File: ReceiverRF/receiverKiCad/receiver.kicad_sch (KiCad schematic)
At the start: 23 parts, among them J2 Conn_01x05_Socket, U1 STM32F103RET6, Y1 YG8M000000S418

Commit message: changement cristal
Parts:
- Y1: value YG8M000000S418 -> CTX853CT-ND; Digikey 3372-YG8M000000S418TR-ND -> CTX853CT-ND
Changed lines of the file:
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@@
 			)
 		)
-		(property "Value" "YG8M000000S418"
+		(property "Value" "CTX853CT-ND"
 			(at 238.76 118.11 0)
 			(effects
@@
 			)
 		)
-		(property "Datasheet" "https://www.digikey.ca/en/products/detail/nextgen-components/YG8M000000S416/17289334"
+		(property "Datasheet" "https://www.digikey.ca/en/products/detail/cts-frequency-controls/406C35D08M00000/2292774"
 			(at 238.76 125.73 0)
 			(effects
@@
 			)
 		)
-		(property "Description" "YG8M000000S416"
+		(property "Description" "406C35D08M00000"
 			(at 238.76 125.73 0)
 			(effects
@@
 			)
 		)
-		(property "Digikey" "  3372-YG8M000000S418TR-ND"
+		(property "Digikey" "CTX853CT-ND"
 			(at 238.76 125.73 0)
 			(effects

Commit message: changement vers footprint 1206
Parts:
- CSTL_C1, CSTL_C2, STM_C1, STM_C3, STM_C4, STM_C5, S_C10, S_C2, S_C7: footprint Capacitor_SMD:C_0402_1005Metric -> Capacitor_SMD:C_1206_3216Metric
- I2C_R1, I2C_R2, STM_R2, STM_R3, S_R1, S_R4: footprint Resistor_SMD:R_0402_1005Metric -> Resistor_SMD:R_1206_3216Metric
- STM_C8, STM_C9: footprint Capacitor_SMD:C_0603_1608Metric -> Capacitor_SMD:C_1206_3216Metric
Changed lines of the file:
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@@
 			)
 		)
-		(property "Footprint" "Resistor_SMD:R_0402_1005Metric"
+		(property "Footprint" "Resistor_SMD:R_1206_3216Metric"
 			(at 240.03 93.218 90)
 			(effects
@@
 			)
 		)
-		(property "Footprint" "Capacitor_SMD:C_0402_1005Metric"
+		(property "Footprint" "Capacitor_SMD:C_1206_3216Metric"
 			(at 248.6152 138.43 0)
 			(effects
@@
 			)
 		)
-		(property "Footprint" "Resistor_SMD:R_0402_1005Metric"
+		(property "Footprint" "Resistor_SMD:R_1206_3216Metric"
 			(at 107.95 56.388 90)
 			(effects
@@
 			)
 		)
-		(property "Footprint" "Resistor_SMD:R_0402_1005Metric"
+		(property "Footprint" "Resistor_SMD:R_1206_3216Metric"
 			(at 230.632 59.69 90)
 			(effects
@@
 			)
 		)
-		(property "Footprint" "Capacitor_SMD:C_0402_1005Metric"
+		(property "Footprint" "Capacitor_SMD:C_1206_3216Metric"
 			(at 97.4852 44.45 0)
 			(effects
@@
 			)
 		)
-		(property "Footprint" "Capacitor_SMD:C_0402_1005Metric"
+		(property "Footprint" "Capacitor_SMD:C_1206_3216Metric"
 			(at 107.6452 44.45 0)
 			(effects
@@
 			)
 		)
-		(property "Footprint" "Resistor_SMD:R_0402_1005Metric"
+		(property "Footprint" "Resistor_SMD:R_1206_3216Metric"
 			(at 244.602 99.06 90)
 			(effects
@@
 			)
 		)
-		(property "Footprint" "Capacitor_SMD:C_0402_1005Metric"
+		(property "Footprint" "Capacitor_SMD:C_1206_3216Metric"
 			(at 232.1052 138.43 0)
 			(effects
@@
 			)
 		)
-		(property "Footprint" "Capacitor_SMD:C_0603_1608Metric"
+		(property "Footprint" "Capacitor_SMD:C_1206_3216Metric"
 			(at 197.8152 44.45 0)
 			(effects
@@
 			)
 		)
-		(property "Footprint" "Capacitor_SMD:C_0603_1608Metric"
+		(property "Footprint" "Capacitor_SMD:C_1206_3216Metric"
 			(at 177.4952 44.45 0)
 			(effects
@@
 			)
 		)
-		(property "Footprint" "Capacitor_SMD:C_0402_1005Metric"
+		(property "Footprint" "Capacitor_SMD:C_1206_3216Metric"
 			(at 117.8052 44.45 0)
 			(effects
@@
 			)
 		)
-		(property "Footprint" "Resistor_SMD:R_0402_1005Metric"
+		(property "Footprint" "Resistor_SMD:R_1206_3216Metric"
 			(at 254 127.508 90)
 			(effects
@@
 			)
 		)
-		(property "Footprint" "Capacitor_SMD:C_0402_1005Metric"
+		(property "Footprint" "Capacitor_SMD:C_1206_3216Metric"
 			(at 168.6052 44.45 0)
 			(effects
@@
 			)
 		)
-		(property "Footprint" "Capacitor_SMD:C_0402_1005Metric"
+		(property "Footprint" "Capacitor_SMD:C_1206_3216Metric"
 			(at 116.5352 62.23 0)
 			(effects
@@
 			)
 		)
-		(property "Footprint" "Capacitor_SMD:C_0402_1005Metric"
+		(property "Footprint" "Capacitor_SMD:C_1206_3216Metric"
 			(at 87.3252 44.45 0)
 			(effects
@@
 			)
 		)
-		(property "Footprint" "Capacitor_SMD:C_0402_1005Metric"
+		(property "Footprint" "Capacitor_SMD:C_1206_3216Metric"
 			(at 127.9652 44.45 0)
 			(effects
@@
 			)
 		)
-		(property "Footprint" "Resistor_SMD:R_0402_1005Metric"
+		(property "Footprint" "Resistor_SMD:R_1206_3216Metric"
 			(at 240.792 59.69 90)
 			(effects

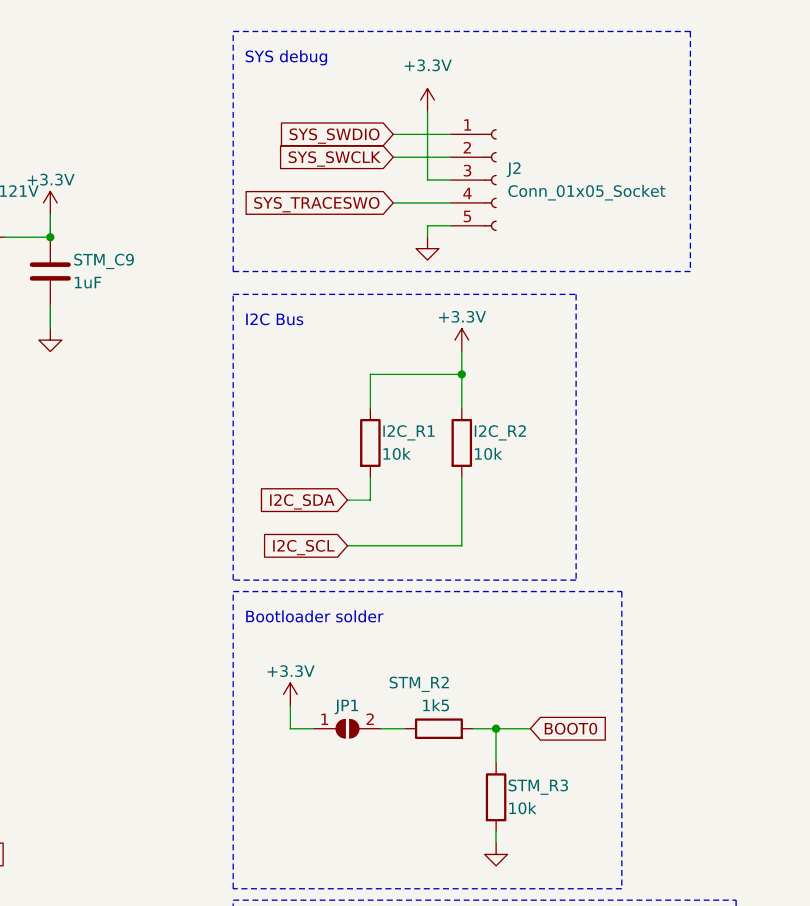
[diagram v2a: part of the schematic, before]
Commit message: changement BOM et choix nouvelles pièces 1206
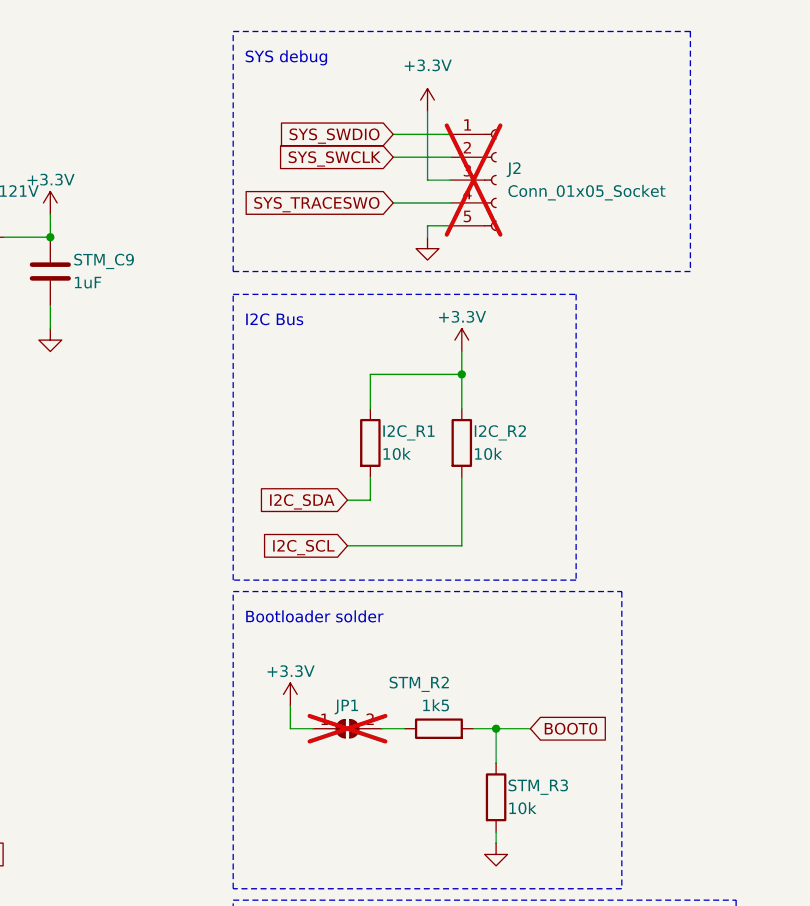
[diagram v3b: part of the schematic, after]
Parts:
- CSTL_C1, CSTL_C2: footprint Capacitor_SMD:C_1206_3216Metric -> Capacitor_SMD:C_0603_1608Metric_Pad1.08x0.95mm_HandSolder; Digikey 478-11769-1-ND -> 399-CBR06C160F5GACCT-ND
- I2C_R1, I2C_R2, STM_R3, S_R1: Digikey 311-10KJRCT-ND -> 311-10.0KFRCT-ND
- J2, JP1: now not fitted
- STM_C1, STM_C3, STM_C4, STM_C5, S_C10, S_C2: Digikey 2679-AGC0402X7R500-104KNPTR-ND -> 399-C1206C104K5RACTUCT-ND
- STM_C8, STM_C9: Digikey 2679-AGC0603X7R250-105KXPTR-ND -> 1276-1068-1-ND
- STM_R2: Digikey P1.5KDCCT-ND -> 541-4184-1-ND
- S_C7: Digikey 2679-AGC0402X7R500-103KNPTR-ND -> 311-1174-1-ND
- S_R4: Digikey P10.0LCT-ND -> RMCF1206FT10R0CT-ND
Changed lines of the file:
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@@
 			)
 		)
-		(property "Digikey" "P1.5KDCCT-ND"
+		(property "Digikey" "541-4184-1-ND"
 			(at 240.03 91.44 0)
 			(effects
@@
 			)
 		)
-		(property "Footprint" "Capacitor_SMD:C_1206_3216Metric"
+		(property "Footprint" "Capacitor_SMD:C_0603_1608Metric_Pad1.08x0.95mm_HandSolder"
 			(at 248.6152 138.43 0)
 			(effects
@@
 			)
 		)
-		(property "Digikey" "478-11769-1-ND"
+		(property "Digikey" "399-CBR06C160F5GACCT-ND"
 			(at 247.65 134.62 0)
 			(effects
@@
 			)
 		)
-		(property "Digikey" "311-10KJRCT-ND"
+		(property "Digikey" "311-10.0KFRCT-ND"
 			(at 107.95 54.61 0)
 			(effects
@@
 		(in_bom yes)
 		(on_board yes)
-		(dnp no)
+		(dnp yes)
 		(property "Reference" "JP1"
 			(at 229.87 88.9 0)
@@
 			)
 		)
-		(property "Digikey" "311-10KJRCT-ND"
+		(property "Digikey" "311-10.0KFRCT-ND"
 			(at 232.41 59.69 0)
 			(effects
@@
 			)
 		)
-		(property "Digikey" "2679-AGC0402X7R500-104KNPTR-ND"
+		(property "Digikey" "399-C1206C104K5RACTUCT-ND"
 			(at 96.52 40.64 0)
 			(effects
@@
 			)
 		)
-		(property "Digikey" "2679-AGC0402X7R500-104KNPTR-ND"
+		(property "Digikey" "399-C1206C104K5RACTUCT-ND"
 			(at 106.68 40.64 0)
 			(effects
@@
 			)
 		)
-		(property "Digikey" "311-10KJRCT-ND"
+		(property "Digikey" "311-10.0KFRCT-ND"
 			(at 246.38 99.06 0)
 			(effects
@@
 			)
 		)
-		(property "Footprint" "Capacitor_SMD:C_1206_3216Metric"
+		(property "Footprint" "Capacitor_SMD:C_0603_1608Metric_Pad1.08x0.95mm_HandSolder"
 			(at 232.1052 138.43 0)
 			(effects
@@
 			)
 		)
-		(property "Digikey" "478-11769-1-ND"
+		(property "Digikey" "399-CBR06C160F5GACCT-ND"
 			(at 231.14 134.62 0)
 			(effects
@@
 			)
 		)
-		(property "Digikey" "  2679-AGC0603X7R250-105KXPTR-ND"
+		(property "Digikey" "1276-1068-1-ND"
 			(at 196.85 40.64 0)
 			(effects
@@
 			)
 		)
-		(property "Digikey" "  2679-AGC0603X7R250-105KXPTR-ND"
+		(property "Digikey" "1276-1068-1-ND"
 			(at 176.53 40.64 0)
 			(effects
@@
 			)
 		)
-		(property "Digikey" "2679-AGC0402X7R500-104KNPTR-ND"
+		(property "Digikey" "399-C1206C104K5RACTUCT-ND"
 			(at 116.84 40.64 0)
 			(effects
@@
 			)
 		)
-		(property "Digikey" "P10.0LCT-ND"
+		(property "Digikey" "RMCF1206FT10R0CT-ND"
 			(at 254 125.73 0)
 			(effects
@@
 			)
 		)
-		(property "Digikey" "  2679-AGC0402X7R500-103KNPTR-ND"
+		(property "Digikey" "311-1174-1-ND"
 			(at 167.64 40.64 0)
 			(effects
@@
 		(in_bom yes)
 		(on_board yes)
-		(dnp no)
+		(dnp yes)
 		(fields_autoplaced yes)
 		(property "Reference" "J2"
@@
 			)
 		)
-		(property "Digikey" "2679-AGC0402X7R500-104KNPTR-ND"
+		(property "Digikey" "399-C1206C104K5RACTUCT-ND"
 			(at 115.57 58.42 0)
 			(effects
@@
 			)
 		)
-		(property "Digikey" "2679-AGC0402X7R500-104KNPTR-ND"
+		(property "Digikey" "399-C1206C104K5RACTUCT-ND"
 			(at 86.36 40.64 0)
 			(effects
@@
 			)
 		)
-		(property "Digikey" "2679-AGC0402X7R500-104KNPTR-ND"
+		(property "Digikey" "399-C1206C104K5RACTUCT-ND"
 			(at 127 40.64 0)
 			(effects
@@
 			)
 		)
-		(property "Digikey" "311-10KJRCT-ND"
+		(property "Digikey" "311-10.0KFRCT-ND"
 			(at 242.57 59.69 0)
 			(effects

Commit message: ideFIX v2 fix schematic, layout
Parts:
- added J3: Conn_01x02_Socket, Connector_PinHeader_2.54mm:PinHeader_1x02_P2.54mm_Vertical, symbol Connector:Conn_01x02_Socket
- J2: footprint Connector_PinHeader_2.00mm:PinHeader_1x05_P2.00mm_Vertical -> Connector_PinHeader_2.54mm:PinHeader_1x05_P2.54mm_Vertical; now fitted
- JP1: now fitted
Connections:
- net BUZZER: now also U1.43 (PA10); no longer U1.41 (PA8)
- net LED1: now also U1.14 (PA0); no longer U1.43 (PA10)
- net LED2: now also U1.15 (PA1); no longer U1.44 (PA11)
- net LED3: now also U1.16 (PA2); no longer U1.45 (PA12)
- net MLX_INT: now also U1.44 (PA11); no longer U1.50 (PA15)
- net MLX_INT/TRIG: now also U1.45 (PA12); no longer U1.52 (PC11)
- net PUSH_1: now also U1.37 (PC6); no longer U1.33 (PB12)
- net PUSH_2: now also U1.38 (PC7); no longer U1.34 (PB13)
- net PUSH_3: now also U1.39 (PC8); no longer U1.35 (PB14)
- net PUSH_4: now also U1.40 (PC9); no longer U1.36 (PB15)
- net RFM_GPIO1: now also U1.27 (PB1); no longer U1.26 (PB0)
- net RFM_GPIO2: now also U1.26 (PB0); no longer U1.27 (PB1)
- net RFM_GPIO3: now also U1.25 (PC5); no longer U1.28 (PB2)
- net RFM_NIRQ: now also U1.20 (PA4); no longer U1.29 (PB10)
- net RFM_SDN: now also U1.17 (PA3); no longer U1.25 (PC5)
- net SPI_RFM_CS: now also U1.24 (PC4); no longer U1.20 (PA4)
- net UART4_TX: now reaches U1.51 (PC10)
- net UART4_TX: now also J3.1 (Pin_1)
- new net RFM_GPIO4: U1.29 (PB10)
- new net RFM_GPIO5: U1.28 (PB2)
- new net UART4_RX: J3.2 (Pin_2), U1.52 (PC11)
- no-connect marks 25 -> 12
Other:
- sheet IOinterface renamed InterfaceBoard
- sheet regulateurs renamed Power
- note added: "UART out"

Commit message: revision schematic before tracing
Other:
- company: (none) -> GAUL
- title: (none) -> IdeFIX
- moved on the sheet: CSTL_C1, CSTL_C2, I2C_R1, I2C_R2, J2, J3, JP1, STM_R2, STM_R3, S_R4, Y1

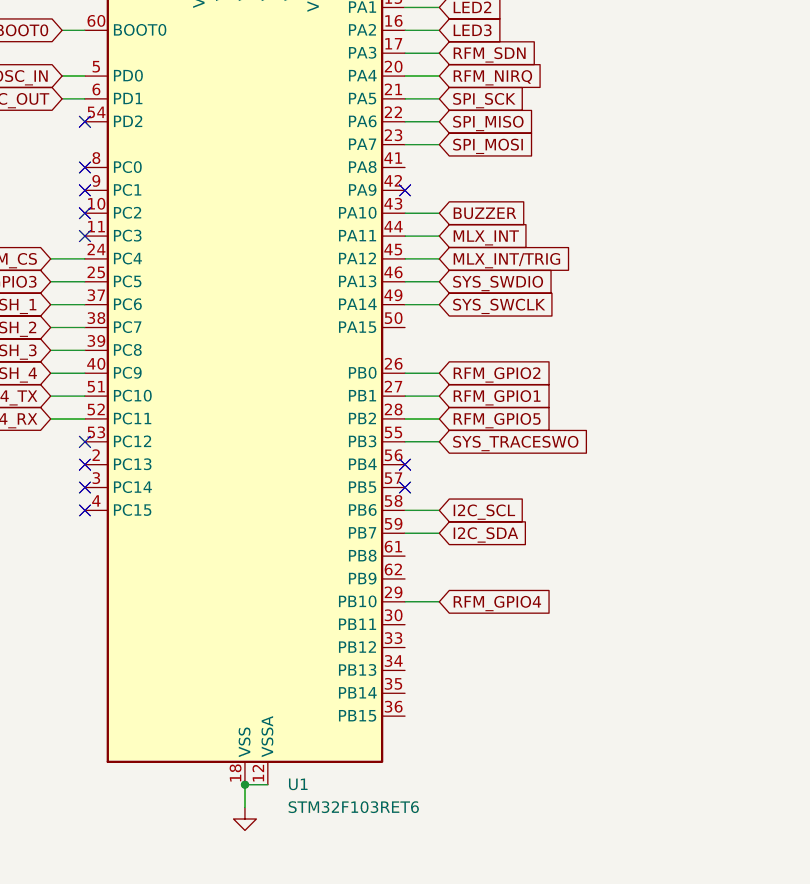
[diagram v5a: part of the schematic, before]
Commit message: fix zener diode footprint, thermal relief on SMA conn, more work on silkscreen
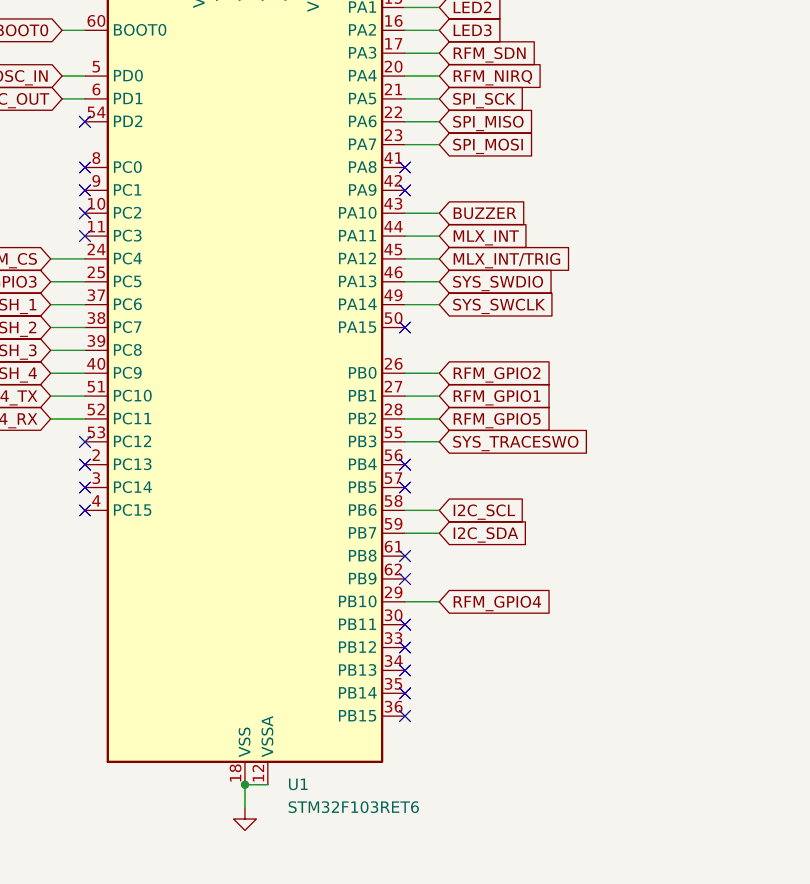
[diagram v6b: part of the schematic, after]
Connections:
- no-connect marks 12 -> 21
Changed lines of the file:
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@@
+	)
+	(no_connect
+		(at 171.45 135.89)
 	)
 	(no_connect
@@
 	)
 	(no_connect
+		(at 171.45 133.35)
+	)
+	(no_connect
+		(at 171.45 120.65)
+	)
+	(no_connect
 		(at 171.45 77.47)
+	)
+	(no_connect
+		(at 171.45 92.71)
 	)
 	(no_connect
@@
 	)
 	(no_connect
+		(at 171.45 130.81)
+	)
+	(no_connect
 		(at 171.45 110.49)
+	)
+	(no_connect
+		(at 171.45 74.93)
 	)
 	(no_connect
@@
 	)
 	(no_connect
+		(at 171.45 125.73)
+	)
+	(no_connect
 		(at 135.89 107.95)
+	)
+	(no_connect
+		(at 171.45 118.11)
 	)
 	(no_connect
@@
 	)
 	(no_connect
+		(at 171.45 128.27)
+	)
+	(no_connect

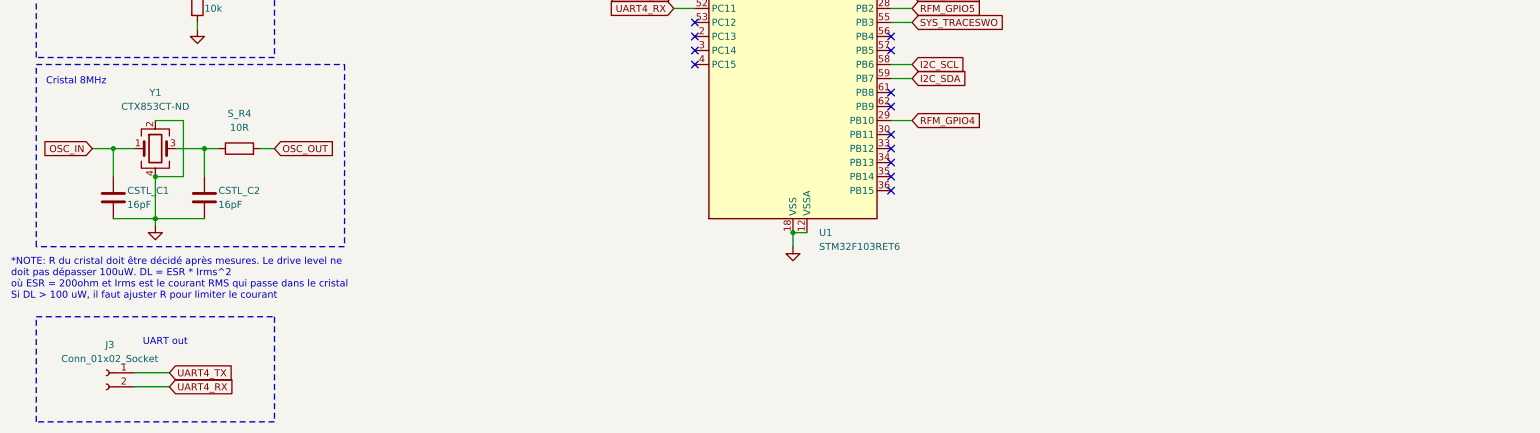
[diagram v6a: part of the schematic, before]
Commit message: 3.2mm holes, XT30 connector, add polyfuse, minor fixes
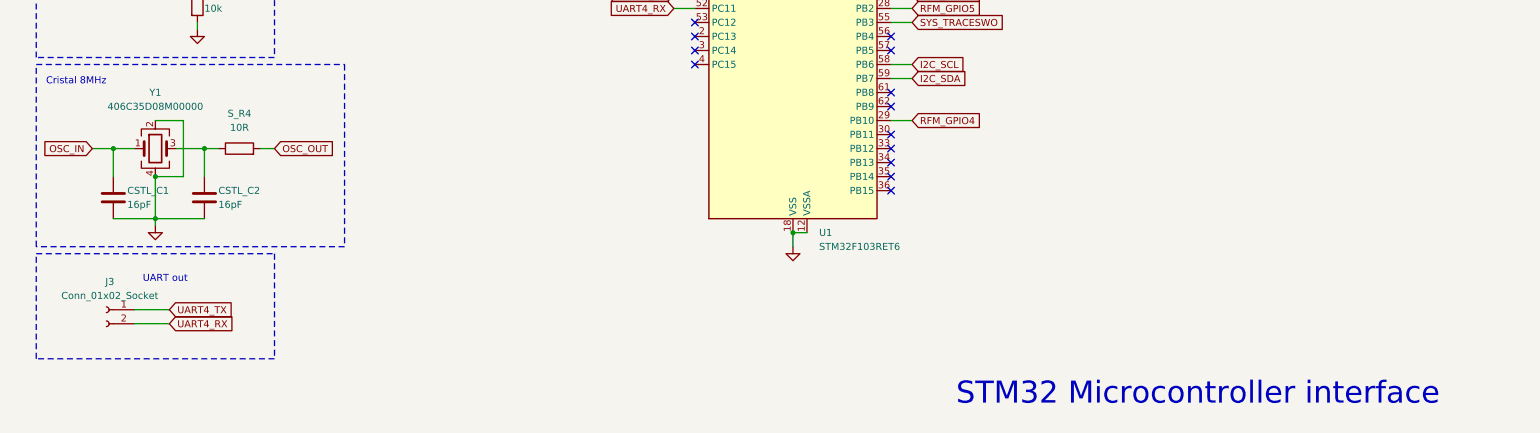
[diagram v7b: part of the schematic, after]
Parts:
- Y1: value CTX853CT-ND -> 406C35D08M00000
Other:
- note added: "STM32 Microcontroller interface"
- note removed: "*NOTE: R du cristal doit être décidé après mesures. Le drive level ne doit pas dépasser 100uW. DL = ESR * Irms^2 où ESR = 200ohm et Irms est le courant RMS qui passe dans le cristal Si DL > 100 uW, il faut ajuster R pour limiter le courant"
- moved on the sheet: J3
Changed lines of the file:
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@@
 	(wire
 		(pts
-			(xy 34.29 168.91) (xy 40.64 168.91)
+			(xy 34.29 157.48) (xy 40.64 157.48)
 		)
 		(stroke
@@
 	(wire
 		(pts
-			(xy 34.29 171.45) (xy 40.64 171.45)
+			(xy 34.29 160.02) (xy 40.64 160.02)
 		)
 		(stroke
@@
 	)
 	(rectangle
-		(start 16.51 158.75)
-		(end 59.69 177.8)
+		(start 16.51 147.32)
+		(end 59.69 166.37)
 		(stroke
 			(width 0)
@@
 		)
 	)
+	(text "STM32 Microcontroller interface"
+		(exclude_from_sim no)
+		(at 227.076 172.72 0)
+		(effects
+			(font
+				(size 4 4)
+			)
+		)
+	)
 	(text "Cristal 8MHz"
 		(exclude_from_sim no)
@@
 		)
 	)
-	(text "*NOTE: R du cristal doit être décidé après mesures. Le drive level ne\ndoit pas dépasser 100uW. DL = ESR * Irms^2\noù ESR = 200ohm et Irms est le courant RMS qui passe dans le cristal\nSi DL > 100 uW, il faut ajuster R pour limiter le courant"
-		(exclude_from_sim no)
-		(at 11.938 151.892 0)
-		(effects
-			(font
-				(size 1.27 1.27)
-			)
-			(justify left)
-		)
-	)
 	(text "UART out\n"
 		(exclude_from_sim no)
-		(at 35.814 164.084 0)
+		(at 35.814 152.654 0)
 		(effects
 			(font
@@
 	(global_label "UART4_RX"
 		(shape input)
-		(at 40.64 171.45 0)
+		(at 40.64 160.02 0)
 		(fields_autoplaced yes)
 		(effects
@@
 		)
 		(property "Intersheetrefs" "${INTERSHEET_REFS}"
-			(at 52.9385 171.45 0)
+			(at 52.9385 160.02 0)
 			(effects
 				(font
@@
 	(global_label "UART4_TX"
 		(shape input)
-		(at 40.64 168.91 0)
+		(at 40.64 157.48 0)
 		(fields_autoplaced yes)
 		(effects
@@
 		)
 		(property "Intersheetrefs" "${INTERSHEET_REFS}"
-			(at 52.6361 168.91 0)
+			(at 52.6361 157.48 0)
 			(effects
 				(font
@@
 	(symbol
 		(lib_id "Connector:Conn_01x02_Socket")
-		(at 29.21 168.91 0)
+		(at 29.21 157.48 0)
 		(mirror y)
 		(unit 1)
@@
 		(fields_autoplaced yes)
 		(property "Reference" "J3"
-			(at 29.845 163.83 0)
+			(at 29.845 152.4 0)
 			(effects
 				(font
@@
 		)
 		(property "Value" "Conn_01x02_Socket"
-			(at 29.845 166.37 0)
+			(at 29.845 154.94 0)
 			(effects
 				(font
@@
 		)
 		(property "Footprint" "Connector_PinHeader_2.54mm:PinHeader_1x02_P2.54mm_Vertical"
-			(at 29.21 168.91 0)
+			(at 29.21 157.48 0)
 			(effects
 				(font
@@
 		)
 		(property "Datasheet" "~"
-			(at 29.21 168.91 0)
+			(at 29.21 157.48 0)
 			(effects
 				(font
@@
 		)
 		(property "Description" "Generic connector, single row, 01x02, script generated"
-			(at 29.21 168.91 0)
+			(at 29.21 157.48 0)
 			(effects
 				(font
@@
 			)
 		)
-		(property "Value" "CTX853CT-ND"
+		(property "Value" "406C35D08M00000"
 			(at 38.1 120.65 0)
 			(effects
